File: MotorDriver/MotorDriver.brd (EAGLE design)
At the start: 50 x 50 mm, 88 parts, among them IC1 DRV8320RSRHAR, IC2 MAX3051ESA+, IC3 TPD4S014DSQR, J1 J_USB_MICROAB_HIROSE_ZX62-AB-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, J2 SM03B-ZESS-TB, Q1 BUK7Y7R8-80EX, Q2 BUK7Y7R8-80EX, Q3 BUK7Y7R8-80EX, Q4 BUK7Y7R8-80EX, Q5 BUK7Y7R8-80EX, Q6 BUK7Y7R8-80EX, U1 LPC1549JBD48, U2 ADCMP350YKSZ, U3 MCP1700T-33, U4 ADR5041, Y1 FA238V

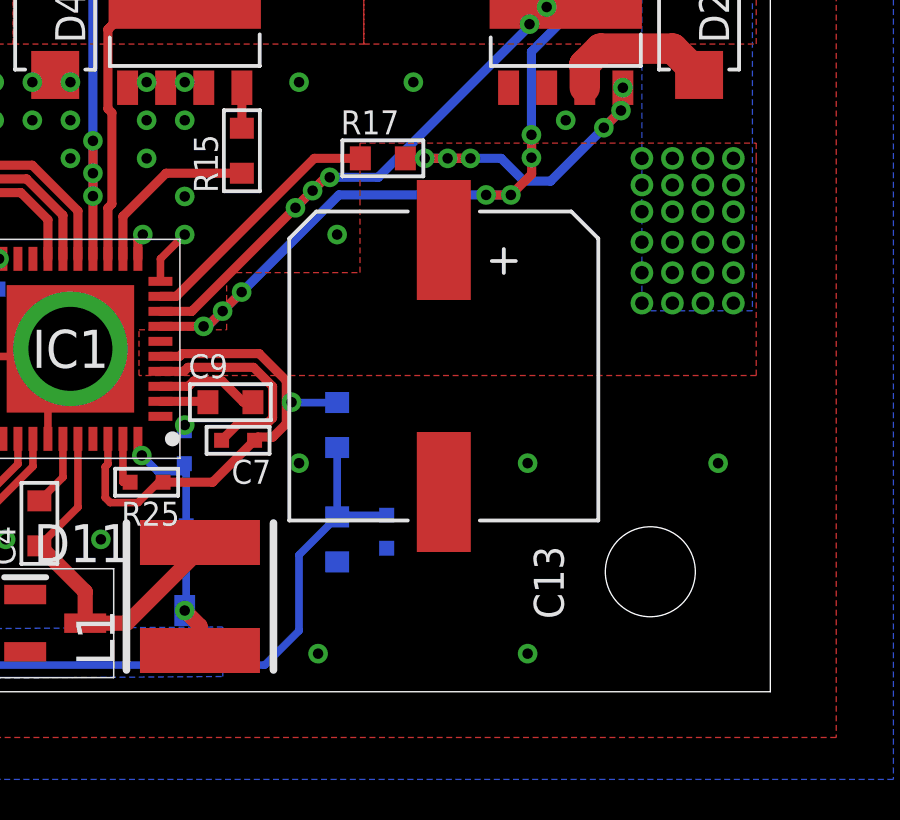
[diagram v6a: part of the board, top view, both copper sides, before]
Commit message: [fix]電源補助コンデンサの容量を小さくした
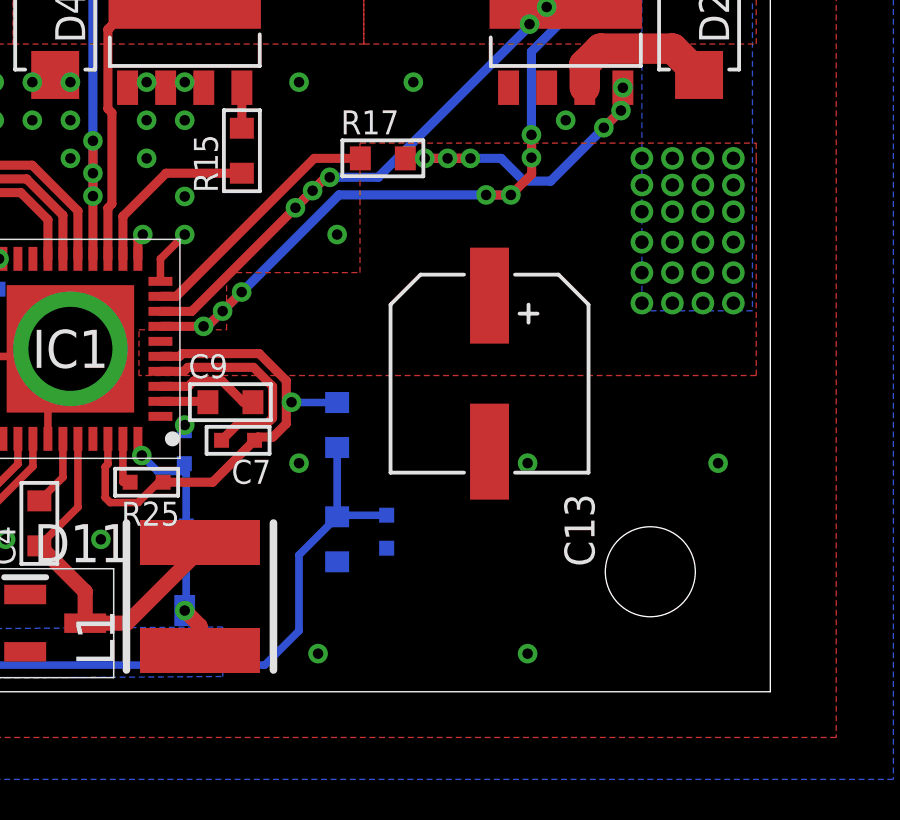
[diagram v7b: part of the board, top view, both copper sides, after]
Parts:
- C13: value 100u -> 22u; device Passive:ES-10 -> Passive:ES-6.3
- moved C13 1.55 mm to (40.6, 10.6)
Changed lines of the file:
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@@
 <?xml version="1.0" encoding="utf-8"?>
 <!DOCTYPE eagle SYSTEM "eagle.dtd">
-<eagle version="8.4.1">
+<eagle version="8.4.3">
 <drawing>
 <settings>
@@
 <element name="SW2" library="MotorDriver" library_urn="urn:adsk.eagle:library:1073580" package="SKRP" package3d_urn="urn:adsk.eagle:package:1073661/2" value="" x="19.177" y="3.81" rot="R180"/>
 <element name="F1" library="Passive" library_urn="urn:adsk.eagle:library:1073310" package="3216" package3d_urn="urn:adsk.eagle:package:1073356/2" value="15" x="17.272" y="40.386" rot="MR180"/>
-<element name="C13" library="Passive" library_urn="urn:adsk.eagle:library:1073310" package="ES-10" package3d_urn="urn:adsk.eagle:package:1073378/1" value="100u" x="39.116" y="10.8585" rot="R270"/>
+<element name="C13" library="Passive" library_urn="urn:adsk.eagle:library:1073310" package="ES-6.3" package3d_urn="urn:adsk.eagle:package:1073376/1" value="22u" x="40.64" y="10.6045" rot="R270"/>
 <element name="R8" library="MotorDriver" library_urn="urn:adsk.eagle:library:1073580" package="R1005" package3d_urn="urn:adsk.eagle:package:1073655/2" value="10k" x="2.667" y="6.35" rot="MR180"/>
 <element name="D13" library="Diode" package="SMPC" value="TSPB20U80S S1G" x="17.145" y="34.798" rot="MR180"/>

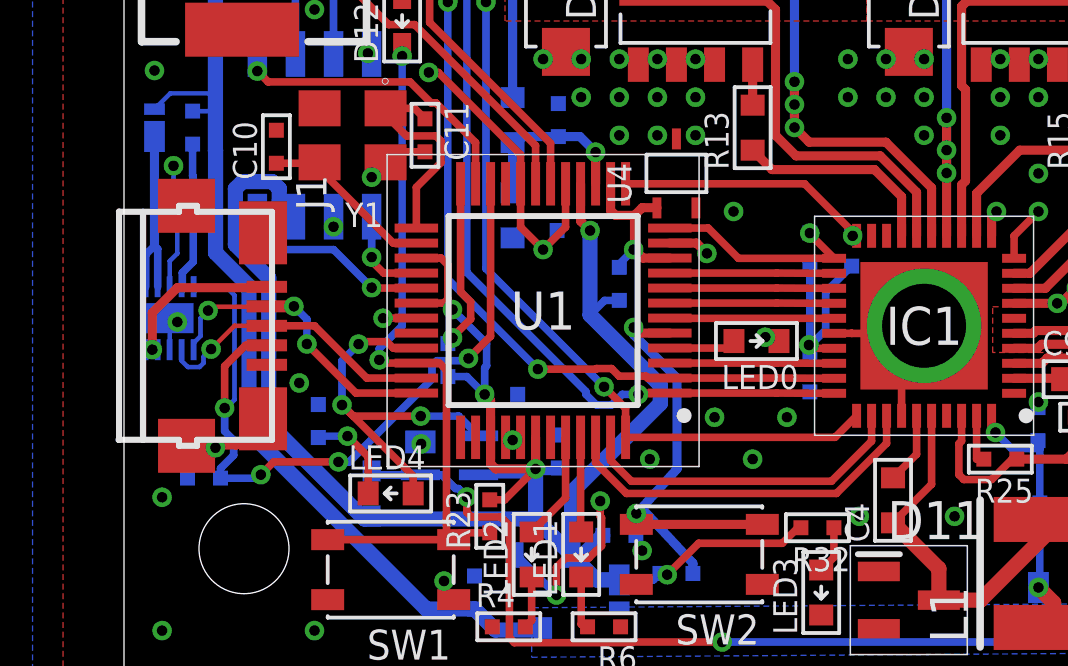
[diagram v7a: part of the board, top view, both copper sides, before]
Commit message: [del]プルアップ/ダウン抵抗を除去
*プルアップ/ダウンにはマイコンの機能を使用することにした
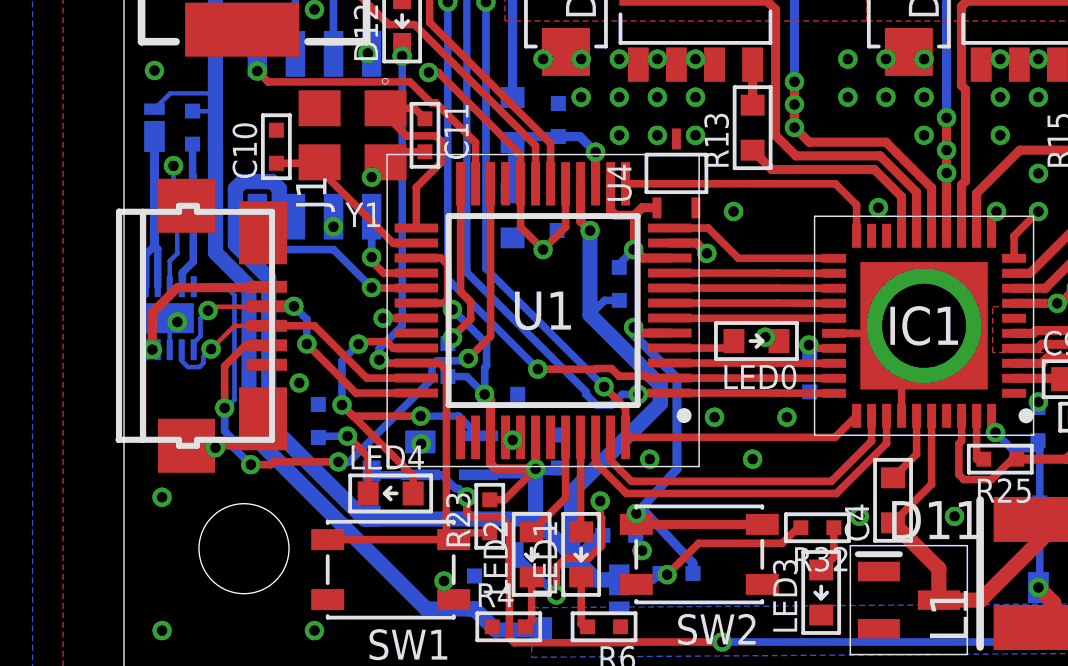
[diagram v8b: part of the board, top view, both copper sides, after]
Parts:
- removed R19, R24, R8: 10k, MotorDriver:R1005
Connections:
- net !FAULT: no longer R24.1
- net GND: no longer R8.1
- net ID: no longer R8.2
- net N$17: no longer R19.2, R24.2
- net SDO: no longer R19.1
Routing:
- net N$17: track 7.25 -> 1.36 mm
- net ID: track 27.5 -> 25.9 mm
- net SDO: track 7.07 -> 5.89 mm, vias 1 -> 0
- net !FAULT: track 8.65 -> 9.02 mm, vias 1 -> 0
- net GND: vias 77 -> 78
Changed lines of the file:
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@@
 <element name="C7" library="MotorDriver" library_urn="urn:adsk.eagle:library:1073580" package="C1005" package3d_urn="urn:adsk.eagle:package:1073645/2" value="1u" x="32.258" y="8.382" rot="R180"/>
 <element name="C8" library="MotorDriver" library_urn="urn:adsk.eagle:library:1073580" package="C1005" package3d_urn="urn:adsk.eagle:package:1073645/2" value="1u" x="22.86" y="9.779" rot="MR270"/>
-<element name="R19" library="MotorDriver" library_urn="urn:adsk.eagle:library:1073580" package="R1005" package3d_urn="urn:adsk.eagle:package:1073655/2" value="10k" x="22.86" y="13.97" rot="MR270"/>
-<element name="R24" library="MotorDriver" library_urn="urn:adsk.eagle:library:1073580" package="R1005" package3d_urn="urn:adsk.eagle:package:1073655/2" value="10k" x="24.257" y="13.97" rot="MR270"/>
 <element name="C9" library="MotorDriver" library_urn="urn:adsk.eagle:library:1073580" package="C1608" package3d_urn="urn:adsk.eagle:package:1073647/2" value="47n" x="32.004" y="9.652"/>
 <element name="R25" library="MotorDriver" library_urn="urn:adsk.eagle:library:1073580" package="R1005" package3d_urn="urn:adsk.eagle:package:1073655/2" value="100k" x="29.21" y="6.985" rot="R180"/>
@@
 <element name="F1" library="Passive" library_urn="urn:adsk.eagle:library:1073310" package="3216" package3d_urn="urn:adsk.eagle:package:1073356/2" value="15" x="17.272" y="40.386" rot="MR180"/>
 <element name="C13" library="Passive" library_urn="urn:adsk.eagle:library:1073310" package="ES-6.3" package3d_urn="urn:adsk.eagle:package:1073376/1" value="22u" x="40.64" y="10.6045" rot="R270"/>
-<element name="R8" library="MotorDriver" library_urn="urn:adsk.eagle:library:1073580" package="R1005" package3d_urn="urn:adsk.eagle:package:1073655/2" value="10k" x="2.667" y="6.35" rot="MR180"/>
 <element name="D13" library="Diode" package="SMPC" value="TSPB20U80S S1G" x="17.145" y="34.798" rot="MR180"/>
 <element name="U2" library="adcmp350" package="KS_4" value="ADCMP350YKSZ" x="10.922" y="7.112" rot="MR90">
@@
 <wire x1="28.92" y1="14.43" x2="28.92" y2="15.077" width="0.3048" layer="1"/>
 <wire x1="28.92" y1="15.077" x2="29.083" y2="15.24" width="0.3048" layer="1"/>
-<contactref element="R8" pad="1"/>
 <via x="8.128" y="20.5105" extent="1-16" drill="0.35" shape="octagon"/>
 <via x="6.35" y="21.971" extent="1-16" drill="0.35" shape="octagon"/>
@@
 <wire x1="10.4775" y1="19.8755" x2="10.16" y2="19.8755" width="0.254" layer="1"/>
 <wire x1="13.22" y1="17.133" x2="10.4775" y2="19.8755" width="0.254" layer="1"/>
+<via x="25.146" y="15.367" extent="1-16" drill="0.35" shape="octagon"/>
 </signal>
 <signal name="+3V3">
@@
 <wire x1="20.483" y1="13.68" x2="23.67" y2="13.68" width="0.254" layer="1"/>
 <wire x1="20.483" y1="13.68" x2="19.475" y2="14.688" width="0.254" layer="1"/>
-<contactref element="R19" pad="1"/>
-<wire x1="23.67" y1="13.68" x2="22.86" y2="14.49" width="0.254" layer="1"/>
-<wire x1="22.86" y1="14.49" x2="22.86" y2="14.52" width="0.254" layer="1"/>
-<via x="22.86" y="14.52" extent="1-16" drill="0.35" shape="octagon"/>
 </signal>
 <signal name="SDI">
@@
 <contactref element="IC1" pad="20"/>
 <contactref element="U1" pad="13"/>
-<contactref element="R24" pad="1"/>
-<wire x1="24.42" y1="14.43" x2="22.687" y2="16.163" width="0.254" layer="1"/>
-<wire x1="22.687" y1="16.163" x2="16.72" y2="16.163" width="0.254" layer="1"/>
-<wire x1="24.257" y1="14.52" x2="24.2902" y2="14.4868" width="0.254" layer="16"/>
-<wire x1="24.2902" y1="14.4868" x2="24.2902" y2="14.43" width="0.254" layer="16"/>
-<via x="24.2902" y="14.43" extent="1-16" drill="0.35" shape="octagon"/>
-<wire x1="24.2902" y1="14.43" x2="24.42" y2="14.43" width="0.254" layer="1"/>
+<wire x1="24.42" y1="15.458" x2="24.42" y2="14.43" width="0.254" layer="1"/>
+<wire x1="16.72" y1="16.163" x2="23.715" y2="16.163" width="0.254" layer="1"/>
+<wire x1="23.715" y1="16.163" x2="24.42" y2="15.458" width="0.254" layer="1"/>
 </signal>
 <signal name="D-">
@@
 <contactref element="IC1" pad="27"/>
 <contactref element="C8" pad="1"/>
-<contactref element="R19" pad="2"/>
-<contactref element="R24" pad="2"/>
-<wire x1="24.257" y1="13.42" x2="23.3894" y2="12.5524" width="0.254" layer="16"/>
 <wire x1="22.86" y1="10.761465625" x2="22.86" y2="10.329" width="0.254" layer="16"/>
 <wire x1="22.86" y1="10.761465625" x2="22.83115" y2="10.790315625" width="0.254" layer="16"/>
@@
 <wire x1="23.67" y1="10.68" x2="22.941465625" y2="10.68" width="0.254" layer="1"/>
 <wire x1="22.941465625" y1="10.68" x2="22.83115" y2="10.790315625" width="0.254" layer="1"/>
-<wire x1="23.3894" y1="11.290865625" x2="22.86" y2="10.761465625" width="0.254" layer="16"/>
-<wire x1="23.3894" y1="12.5524" x2="23.3894" y2="11.290865625" width="0.254" layer="16"/>
-<wire x1="22.86" y1="13.42" x2="22.86" y2="10.761465625" width="0.254" layer="16"/>
 </signal>
 <signal name="N$18">
@@
 <contactref element="J1" pad="P$4"/>
 <contactref element="U1" pad="22"/>
-<contactref element="R8" pad="2"/>
 <wire x1="12.22" y1="16.163" x2="12.22" y2="11.0834625" width="0.254" layer="1"/>
 <wire x1="12.22" y1="11.0834625" x2="11.4803375" y2="10.3438" width="0.254" layer="1"/>
@@
 <via x="7.148275" y="6.894275" extent="1-16" drill="0.35" shape="octagon"/>
 <wire x1="4.049" y1="10.78" x2="4.76" y2="10.78" width="0.254" layer="1"/>
-<wire x1="4.561125" y1="6.466125" x2="4.445" y2="6.35" width="0.254" layer="16"/>
-<via x="4.561125" y="6.466125" extent="1-16" drill="0.35" shape="octagon"/>
 <wire x1="7.148275" y1="6.894275" x2="4.989275" y2="6.894275" width="0.254" layer="1"/>
-<wire x1="4.989275" y1="6.894275" x2="4.561125" y2="6.466125" width="0.254" layer="1"/>
 <contactref element="IC3" pad="5"/>
-<wire x1="4.445" y1="6.35" x2="3.217" y2="6.35" width="0.254" layer="16"/>
-<wire x1="3.6548" y1="7.11465" x2="3.6548" y2="7.61735" width="0.254" layer="16"/>
-<wire x1="3.217" y1="6.35" x2="3.217" y2="6.67685" width="0.254" layer="16"/>
-<wire x1="3.217" y1="6.67685" x2="3.6548" y2="7.11465" width="0.254" layer="16"/>
 <wire x1="3.6548" y1="7.61735" x2="3.3552" y2="7.91695" width="0.254" layer="16"/>
 <wire x1="3.3552" y1="8.636" x2="3.3552" y2="8.6883375" width="0.254" layer="16"/>
@@
 <wire x1="3.683" y1="12.446" x2="3.683" y2="8.9638" width="0.1524" layer="16"/>
 <wire x1="3.683" y1="8.9638" x2="3.3552" y2="8.636" width="0.1524" layer="16"/>
+<wire x1="4.989275" y1="6.894275" x2="4.8952" y2="6.8002" width="0.254" layer="1"/>
+<wire x1="4.8952" y1="6.8002" x2="4.22705" y2="6.8002" width="0.254" layer="1"/>
+<via x="4.22705" y="6.8002" extent="1-16" drill="0.35" shape="octagon"/>
+<wire x1="4.22705" y1="6.8002" x2="3.6548" y2="7.37245" width="0.254" layer="16"/>
+<wire x1="3.6548" y1="7.37245" x2="3.6548" y2="7.61735" width="0.254" layer="16"/>
 </signal>
 <signal name="N$23">
